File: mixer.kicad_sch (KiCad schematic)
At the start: 24 parts, among them U1 TS5A63157DBV, U2 TS5A63157DBV, U4 4051

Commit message: modify mixer.kicad_sch
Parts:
- added C10: 100nF, symbol Device:C_Small
- added C9: 1uF, symbol Device:C_Small
- C1, C3, C5, C7: value 2n2 -> 22nF; JLCPCB (none) -> C21122
- C2, C4, C6, C8: footprint (none) -> Capacitor_Tantalum_SMD:CP_EIA-3216-18_Kemet-A_Pad1.58x1.35mm_HandSolder; JLCPCB (none) -> C123294
- R1: footprint (none) -> Resistor_SMD:R_0603_1608Metric_Pad0.98x0.95mm_HandSolder; JLCPCB (none) -> C22950
- R2, R3, R4: JLCPCB (none) -> C22950
- U1, U2: value TS5A63157DBV -> SN74LVC1G3157DBVR; JLCPCB (none) -> C10426
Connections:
- net GND: now also U1.2 (GND), U2.2 (GND), C10.1, C9.1
- net J90: now reaches U1.6
- net +3.3V: now reaches U1.5 (V+)
- net +3.3V: now also U2.5 (V+), C10.2, C9.2
- net J0: now reaches U2.6

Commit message: schematics mixer progress, 74HC4053, IF RX. PCB update
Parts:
- removed C1: 820(390)pF, LCSDR:C_Disc_D7.5mm_W2.5mm_P5.00mm, symbol C_Small
- removed C15, C36, C73: 100nF, Capacitors_SMD:C_0603_HandSoldering, symbol C_Small
- removed C28: 10uF, Capacitors_THT:CP_Radial_D5.0mm_P2.00mm, symbol CP_Small
- removed L1: 1(0.47)uH, LCSDR:R_Axial_DIN0207_L6.3mm_D2.5mm_P10.16mm_Horizontal, symbol L_Small
- removed L15: 100uH, Resistors_THT:R_Axial_DIN0204_L3.6mm_D1.6mm_P7.62mm_Horizontal, symbol L_Small
- removed R53, R54: 510R, LCSDR:R_1206_0603, symbol R_Small
- removed U4: 4051, Housings_SSOP:TSSOP-16_4.4x5mm_Pitch0.65mm, symbol 4051
- added C11, C13: 100nF, Capacitor_SMD:C_0603_1608Metric_Pad1.08x0.95mm_HandSolder, symbol Device:C_Small
- added C12: 10uF, Capacitor_Tantalum_SMD:CP_EIA-3216-18_Kemet-A_Pad1.58x1.35mm_HandSolder, symbol Device:C_Polarized_Small
- added L1, L2: 100uH, Inductor_SMD:L_1210_3225Metric_Pad1.42x2.65mm_HandSolder, symbol Device:L_Small
- added R5, R6: 1k, Resistor_SMD:R_0603_1608Metric_Pad0.98x0.95mm_HandSolder, symbol Device:R_Small
- C10, C9: footprint (none) -> Capacitor_SMD:C_0603_1608Metric_Pad1.08x0.95mm_HandSolder
- C5: value 22nF -> 2.2nF
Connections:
- net +3.3V: now also L1.1, R5.1; no longer C10.2, C9.2, U1.5 (V+), U2.5 (V+)
- net GND: now also C11.1, C12.2, R6.2
- net J0: now also U1.6; no longer U2.6
- net J90: now also U2.6; no longer U1.6
- net P0: no longer C2.1, C6.1, C8.1
- net at U1.4, U2.4: now also C13.2, L2.2
- new net: C10.2, C9.2, L1.2, U1.5 (V+), U2.5 (V+)
- new net: C11.2, C12.1, L2.1, R5.2, R6.1
- new net BPF: C13.1
- new net P180: C2.1
- new net P270: C6.1
- new net P90: C8.1
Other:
- moved on the sheet: C1, C10, C2, C3, C4, C5, C6, C7, C8, C9, R1, R2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

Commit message: schematics mixer, 74HC4053. IF RX needs JLCPCB numbers. PCB update
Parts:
- C1, C3, C7: value 22nF -> 2.2nF; JLCPCB C21122 -> C1604
- C10, C11, C13: JLCPCB (none) -> C14663
- C5: JLCPCB C21122 -> C1604
- C9: JLCPCB (none) -> C15849
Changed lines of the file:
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@@
+			)
+		)
+		(property "JLCPCB" "C14663"
+			(at 165.1 76.2 90)
+			(effects
+				(font
+					(size 1.524 1.524)
+				)
+				(hide yes)
 			)
 		)
@@
 			)
 		)
-		(property "JLCPCB" "C21122"
+		(property "JLCPCB" "C1604"
 			(at 229.87 77.47 0)
 			(effects
@@
 			)
 		)
-		(property "Value" "22nF"
+		(property "Value" "2.2nF"
 			(at 232.41 60.9662 0)
 			(effects
@@
 			)
 		)
-		(property "JLCPCB" "C21122"
+		(property "JLCPCB" "C1604"
 			(at 229.87 59.69 0)
 			(effects
@@
 			)
 		)
-		(property "Value" "22nF"
+		(property "Value" "2.2nF"
 			(at 232.41 95.2562 0)
 			(effects
@@
 			)
 		)
-		(property "JLCPCB" "C21122"
+		(property "JLCPCB" "C1604"
 			(at 229.87 93.98 0)
 			(effects
@@
 				(font
 					(size 1.27 1.27)
+				)
+				(hide yes)
+			)
+		)
+		(property "JLCPCB" "C15849"
+			(at 41.91 157.48 90)
+			(effects
+				(font
+					(size 1.524 1.524)
 				)
 				(hide yes)
@@
 			)
 		)
-		(property "Value" "22nF"
+		(property "Value" "2.2nF"
 			(at 232.41 41.9162 0)
 			(effects
@@
 			)
 		)
-		(property "JLCPCB" "C21122"
+		(property "JLCPCB" "C1604"
 			(at 229.87 40.64 0)
 			(effects
@@
 			)
 		)
+		(property "JLCPCB" "C14663"
+			(at 133.35 54.61 0)
+			(effects
+				(font
+					(size 1.524 1.524)
+				)
+				(hide yes)
+			)
+		)
 		(pin "2"
 		)
@@
 				)
 				(hide yes)
+			)
+		)
+		(property "JLCPCB" "C14663"
+			(at 81.28 157.48 90)
+			(effects
+				(font
+					(size 1.524 1.524)
+				)
+				(hide yes)

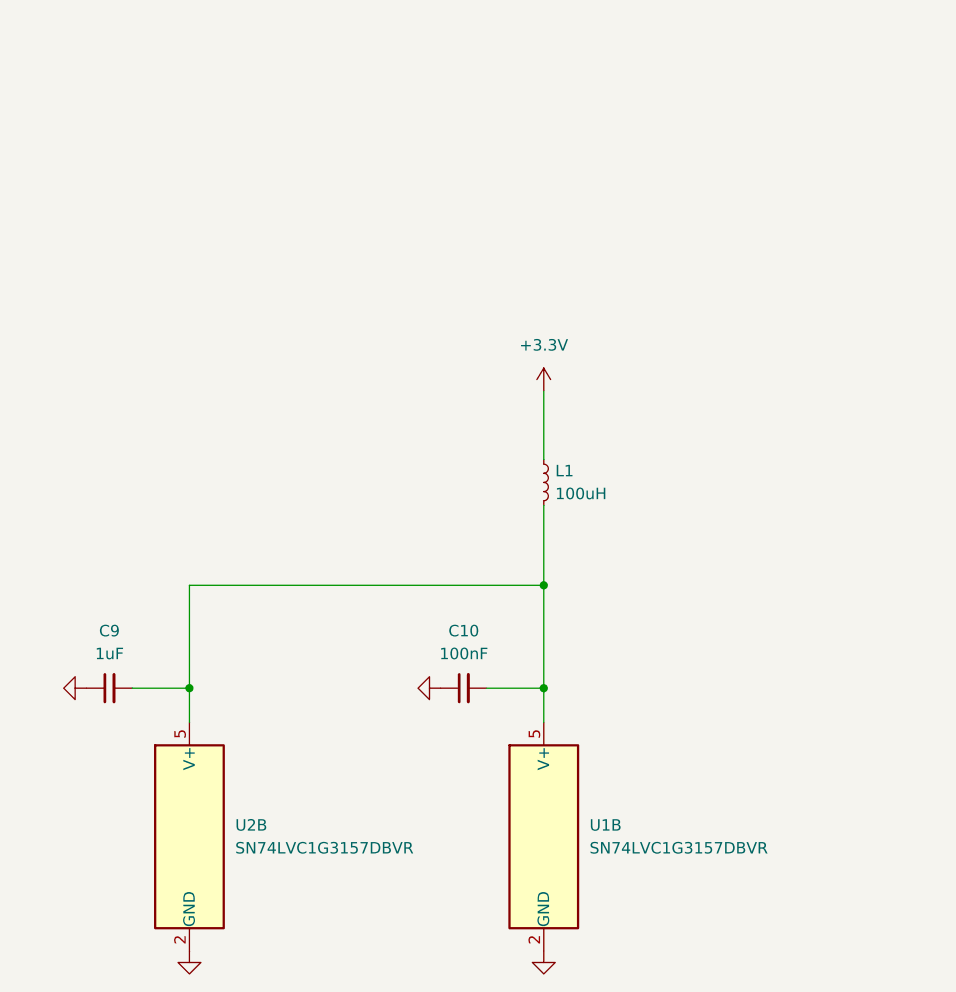
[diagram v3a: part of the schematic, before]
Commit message: finich IF_RX_Schematics, begin MCU, delete *.sch files
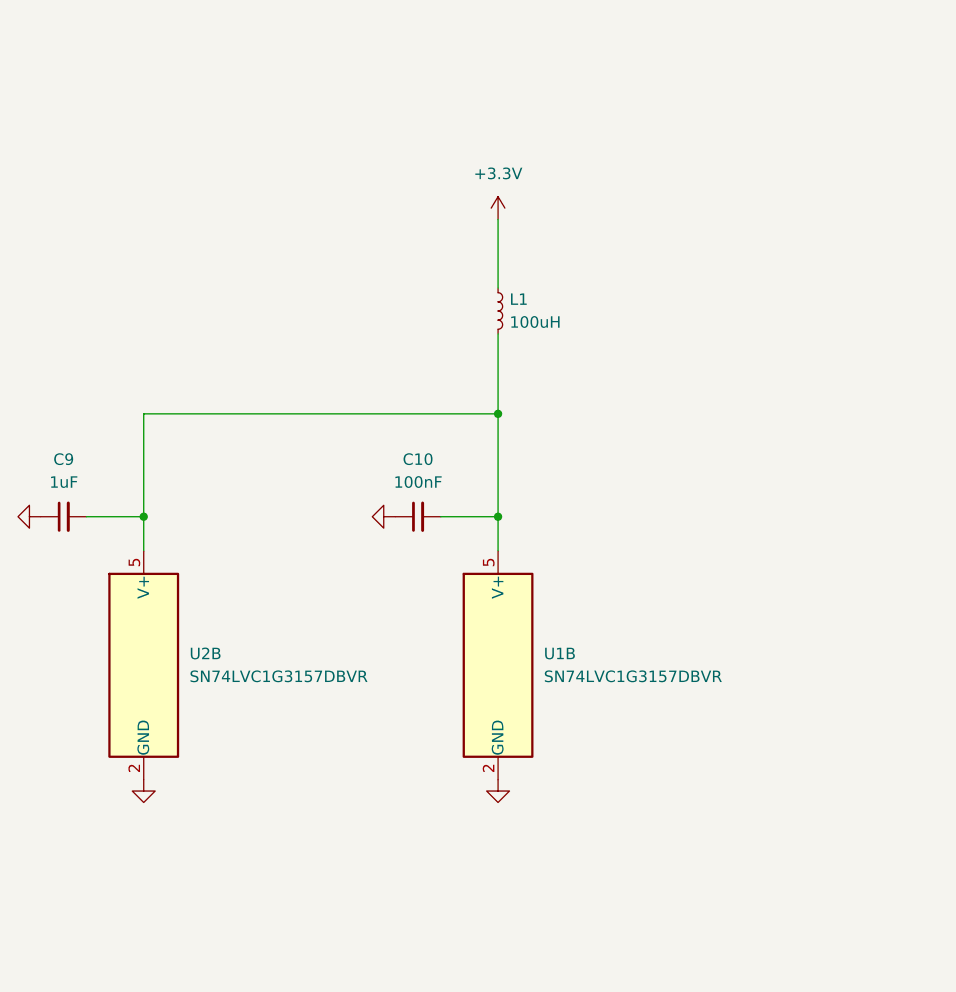
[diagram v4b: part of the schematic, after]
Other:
- moved on the sheet: C10, C9, L1, U1B, U2B

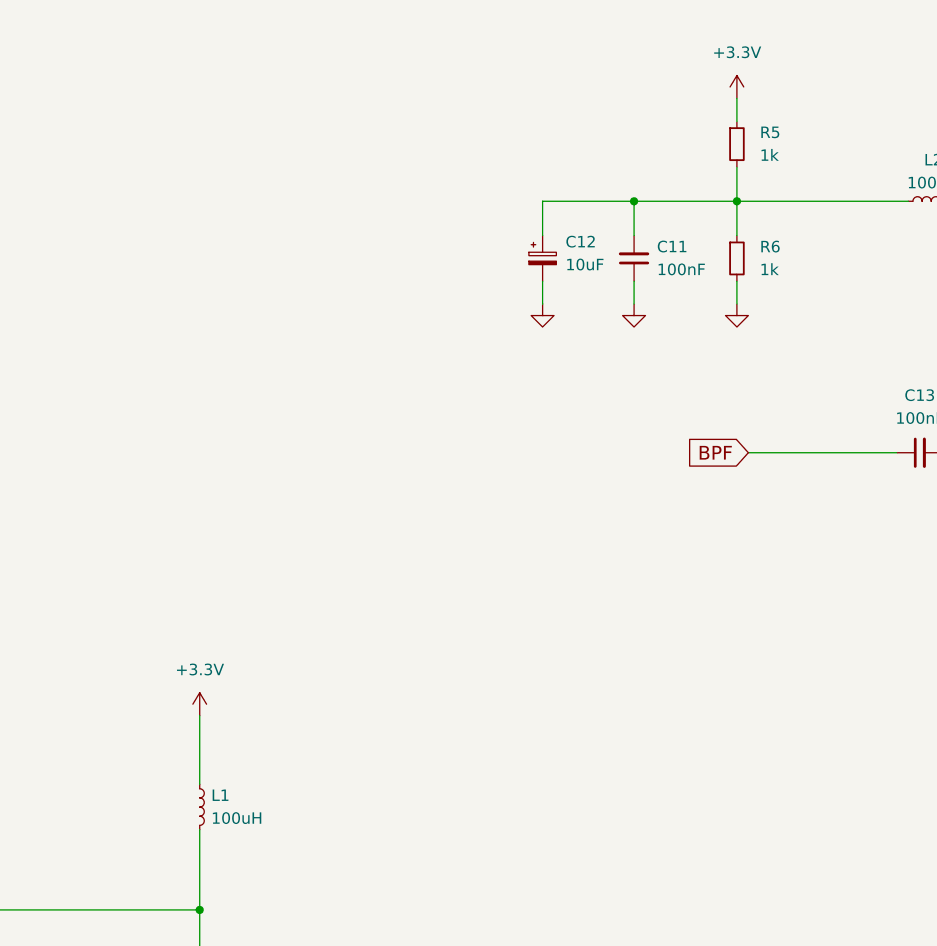
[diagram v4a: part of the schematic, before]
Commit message: schematics mixer progress, mcu
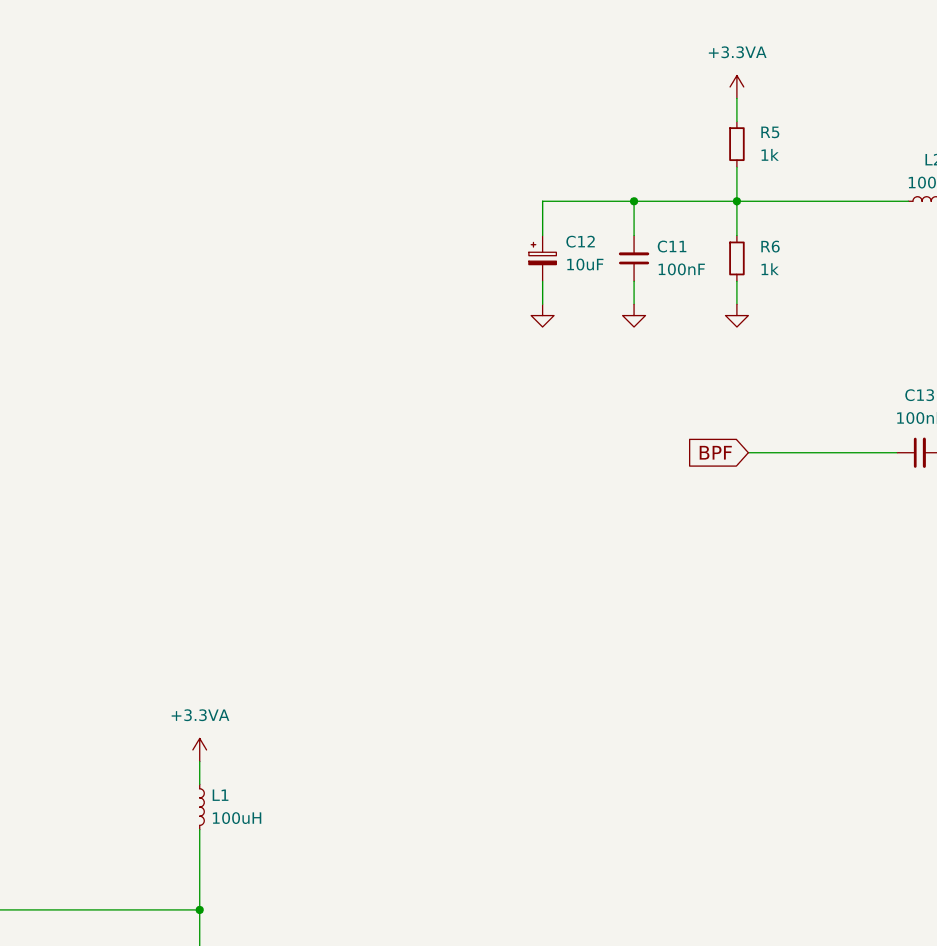
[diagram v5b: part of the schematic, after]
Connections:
- net +3.3V renamed +3.3VA
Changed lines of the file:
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@@
 	(wire
 		(pts
-			(xy 85.09 105.41) (xy 85.09 113.03)
+			(xy 85.09 110.49) (xy 85.09 113.03)
 		)
 		(stroke
@@
 	)
 	(symbol
-		(lib_id "power:+3.3V")
-		(at 85.09 105.41 0)
-		(unit 1)
-		(exclude_from_sim no)
-		(in_bom yes)
-		(on_board yes)
-		(dnp no)
-		(fields_autoplaced yes)
-		(property "Reference" "#PWR010"
-			(at 85.09 109.22 0)
-			(effects
-				(font
-					(size 1.27 1.27)
-				)
-				(hide yes)
-			)
-		)
-		(property "Value" "+3.3V"
-			(at 85.09 100.33 0)
-			(effects
-				(font
-					(size 1.27 1.27)
-				)
-			)
-		)
-		(property "Footprint" ""
-			(at 85.09 105.41 0)
-			(effects
-				(font
-					(size 1.27 1.27)
-				)
-				(hide yes)
-			)
-		)
-		(property "Datasheet" ""
-			(at 85.09 105.41 0)
-			(effects
-				(font
-					(size 1.27 1.27)
-				)
-				(hide yes)
-			)
-		)
-		(property "Description" "Power symbol creates a global label with name \"+3.3V\""
-			(at 85.09 105.41 0)
-			(effects
-				(font
-					(size 1.27 1.27)
-				)
-				(hide yes)
-			)
-		)
-		(pin "1"
-		)
-		(instances
-			(project "pure"
-				(path "/74d736cc-15c3-4dc5-ae3c-dc08a689d728/00000000-0000-0000-0000-0000615c99b7"
-					(reference "#PWR010")
-					(unit 1)
-				)
-			)
-		)
-	)
-	(symbol
 		(lib_id "Device:C_Polarized_Small")
 		(at 240.03 54.61 270)
@@
 	)
 	(symbol
+		(lib_id "power:+3.3VA")
+		(at 144.78 36.83 0)
+		(unit 1)
+		(exclude_from_sim no)
+		(in_bom yes)
+		(on_board yes)
+		(dnp no)
+		(fields_autoplaced yes)
+		(property "Reference" "#PWR010"
+			(at 144.78 40.64 0)
+			(effects
+				(font
+					(size 1.27 1.27)
+				)
+				(hide yes)
+			)
+		)
+		(property "Value" "+3.3VA"
+			(at 144.78 31.75 0)
+			(effects
+				(font
+					(size 1.27 1.27)
+				)
+			)
+		)
+		(property "Footprint" ""
+			(at 144.78 36.83 0)
+			(effects
+				(font
+					(size 1.27 1.27)
+				)
+				(hide yes)
+			)
+		)
+		(property "Datasheet" ""
+			(at 144.78 36.83 0)
+			(effects
+				(font
+					(size 1.27 1.27)
+				)
+				(hide yes)
+			)
+		)
+		(property "Description" "Power symbol creates a global label with name \"+3.3VA\""
+			(at 144.78 36.83 0)
+			(effects
+				(font
+					(size 1.27 1.27)
+				)
+				(hide yes)
+			)
+		)
+		(pin "1"
+		)
+		(instances
+			(project "pure"
+				(path "/74d736cc-15c3-4dc5-ae3c-dc08a689d728/00000000-0000-0000-0000-0000615c99b7"
+					(reference "#PWR010")
+					(unit 1)
+				)
+			)
+		)
+	)
+	(symbol
 		(lib_id "Device:R_Small")
 		(at 144.78 41.91 0)
@@
 				(path "/74d736cc-15c3-4dc5-ae3c-dc08a689d728/00000000-0000-0000-0000-0000615c99b7"
 					(reference "C8")
+					(unit 1)
+				)
+			)
+		)
+	)
+	(symbol
+		(lib_id "power:+3.3VA")
+		(at 85.09 110.49 0)
+		(unit 1)
+		(exclude_from_sim no)
+		(in_bom yes)
+		(on_board yes)
+		(dnp no)
+		(fields_autoplaced yes)
+		(property "Reference" "#PWR040"
+			(at 85.09 114.3 0)
+			(effects
+				(font
+					(size 1.27 1.27)
+				)
+				(hide yes)
+			)
+		)
+		(property "Value" "+3.3VA"
+			(at 85.09 105.41 0)
+			(effects
+				(font
+					(size 1.27 1.27)
+				)
+			)
+		)
+		(property "Footprint" ""
+			(at 85.09 110.49 0)
+			(effects
+				(font
+					(size 1.27 1.27)
+				)
+				(hide yes)
+			)
+		)
+		(property "Datasheet" ""
+			(at 85.09 110.49 0)
+			(effects
+				(font
+					(size 1.27 1.27)
+				)
+				(hide yes)
+			)
+		)
+		(property "Description" "Power symbol creates a global label with name \"+3.3VA\""
+			(at 85.09 110.49 0)
+			(effects
+				(font
+					(size 1.27 1.27)
+				)
+				(hide yes)
+			)
+		)
+		(pin "1"
+		)
+		(instances
+			(project "pure"
+				(path "/74d736cc-15c3-4dc5-ae3c-dc08a689d728/00000000-0000-0000-0000-0000615c99b7"
+					(reference "#PWR040")
 					(unit 1)
 				)
@@
 					(unit 1)
 				)
-			)
-		)
-	)
-	(symbol
-		(lib_id "power:+3.3V")
-		(at 144.78 36.83 0)
-		(unit 1)
-		(exclude_from_sim no)
-		(in_bom yes)
-		(on_board yes)
-		(dnp no)
-		(fields_autoplaced yes)
-		(property "Reference" "#PWR09"
-			(at 144.78 40.64 0)
-			(effects
-				(font
-					(size 1.27 1.27)
-				)
-				(hide yes)
-			)
-		)
-		(property "Value" "+3.3V"
-			(at 144.78 31.75 0)
-			(effects
-				(font
-					(size 1.27 1.27)
-				)
-			)
-		)
-		(property "Footprint" ""
-			(at 144.78 36.83 0)
-			(effects
-				(font
-					(size 1.27 1.27)
-				)
-				(hide yes)
-			)
-		)
-		(property "Datasheet" ""
-			(at 144.78 36.83 0)
-			(effects
-				(font
-					(size 1.27 1.27)
-				)
-				(hide yes)
-			)
-		)
-		(property "Description" "Power symbol creates a global label with name \"+3.3V\""
-			(at 144.78 36.83 0)
-			(effects
-				(font
-					(size 1.27 1.27)
-				)
-				(hide yes)
-			)
-		)
-		(pin "1"
-		)
-		(instances
-			(project "pure"
-				(path "/74d736cc-15c3-4dc5-ae3c-dc08a689d728/00000000-0000-0000-0000-0000615c99b7"
-					(reference "#PWR09")
-					(unit 1)
-				)

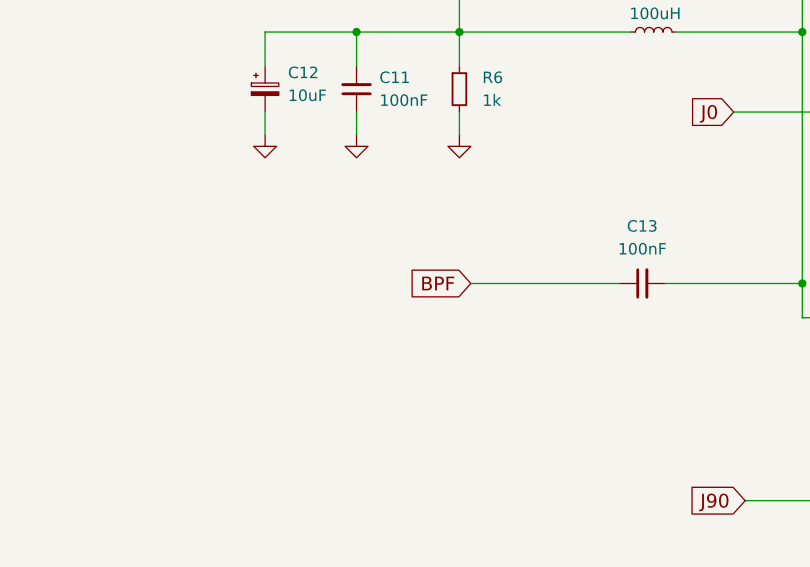
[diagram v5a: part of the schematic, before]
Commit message: 10_17M BPF done
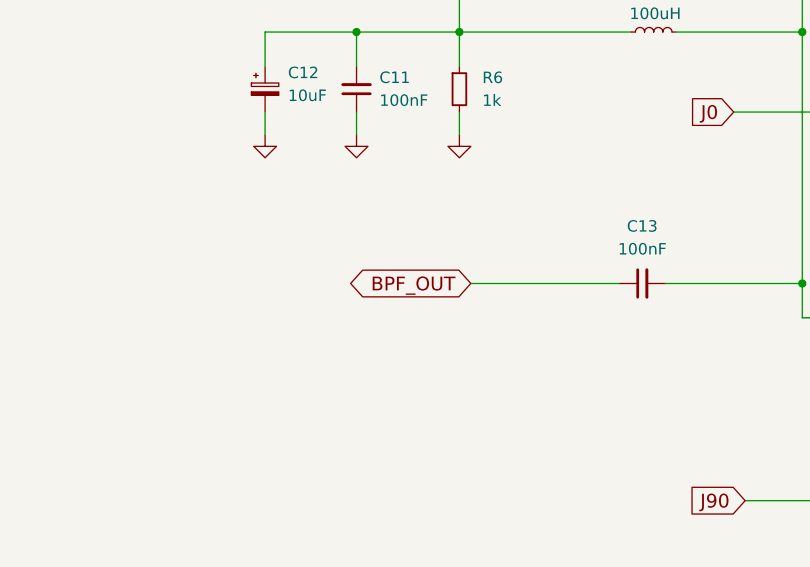
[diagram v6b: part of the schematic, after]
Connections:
- net BPF renamed BPF_OUT
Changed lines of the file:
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@@
 		)
 	)
-	(global_label "BPF"
-		(shape input)
+	(global_label "BPF_OUT"
+		(shape bidirectional)
 		(at 146.05 76.2 180)
 		(fields_autoplaced yes)
@@
 		)
 		(property "Intersheetrefs" "${INTERSHEET_REFS}"
-			(at 138.8989 76.2 0)
+			(at 132.2405 76.2 0)
 			(effects
 				(font

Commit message: progress on PCB
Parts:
- C1, C3, C5, C7: footprint (none) -> SDR_footprints:C_1206_0603
- L1, L2: footprint Inductor_SMD:L_1210_3225Metric_Pad1.42x2.65mm_HandSolder -> Inductor_THT:L_Axial_L5.3mm_D2.2mm_P10.16mm_Horizontal_Vishay_IM-1
- R1: footprint Resistor_SMD:R_0603_1608Metric_Pad0.98x0.95mm_HandSolder -> SDR_footprints:R_1206_0603
- R2, R3, R4: footprint (none) -> SDR_footprints:R_1206_0603
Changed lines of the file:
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@@
 			)
 		)
-		(property "Footprint" ""
+		(property "Footprint" "SDR_footprints:C_1206_0603"
 			(at 229.87 77.47 0)
 			(effects
@@
 			)
 		)
-		(property "Footprint" ""
+		(property "Footprint" "SDR_footprints:C_1206_0603"
 			(at 229.87 59.69 0)
 			(effects
@@
 			)
 		)
-		(property "Footprint" ""
+		(property "Footprint" "SDR_footprints:C_1206_0603"
 			(at 229.87 93.98 0)
 			(effects
@@
 			)
 		)
-		(property "Footprint" ""
+		(property "Footprint" "SDR_footprints:R_1206_0603"
 			(at 222.25 54.61 0)
 			(effects
@@
 			)
 		)
-		(property "Footprint" ""
+		(property "Footprint" "SDR_footprints:R_1206_0603"
 			(at 222.25 88.9 0)
 			(effects
@@
 			)
 		)
-		(property "Footprint" "Inductor_SMD:L_1210_3225Metric_Pad1.42x2.65mm_HandSolder"
+		(property "Footprint" "Inductor_THT:L_Axial_L5.3mm_D2.2mm_P10.16mm_Horizontal_Vishay_IM-1"
 			(at 85.09 115.57 0)
 			(effects
@@
 			)
 		)
-		(property "Footprint" ""
+		(property "Footprint" "SDR_footprints:C_1206_0603"
 			(at 229.87 40.64 0)
 			(effects
@@
 			)
 		)
-		(property "Footprint" "Inductor_SMD:L_1210_3225Metric_Pad1.42x2.65mm_HandSolder"
+		(property "Footprint" "Inductor_THT:L_Axial_L5.3mm_D2.2mm_P10.16mm_Horizontal_Vishay_IM-1"
 			(at 166.37 48.26 0)
 			(effects
@@
 			)
 		)
-		(property "Footprint" "Resistor_SMD:R_0603_1608Metric_Pad0.98x0.95mm_HandSolder"
+		(property "Footprint" "SDR_footprints:R_1206_0603"
 			(at 222.25 35.56 0)
 			(effects
@@
 			)
 		)
-		(property "Footprint" ""
+		(property "Footprint" "SDR_footprints:R_1206_0603"
 			(at 222.25 72.39 0)
 			(effects

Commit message: progress on schematics and pcb
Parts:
- C13: footprint Capacitor_SMD:C_0603_1608Metric_Pad1.08x0.95mm_HandSolder -> SDR_footprints:C_1206_0603
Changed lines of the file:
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@@
 			)
 		)
-		(property "Footprint" "Capacitor_SMD:C_0603_1608Metric_Pad1.08x0.95mm_HandSolder"
+		(property "Footprint" "SDR_footprints:C_1206_0603"
 			(at 165.1 76.2 0)
 			(effects
